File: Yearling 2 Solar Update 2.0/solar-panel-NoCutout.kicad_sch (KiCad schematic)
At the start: 27 parts, among them J1 CON-5040500591, J2 Conn_01x01, J3 Conn_01x01, J4 Conn_01x01, J5 Conn_01x01, U1 APDS-9960, U2 MCP9808_DFN, U3 DRV2605LDGS

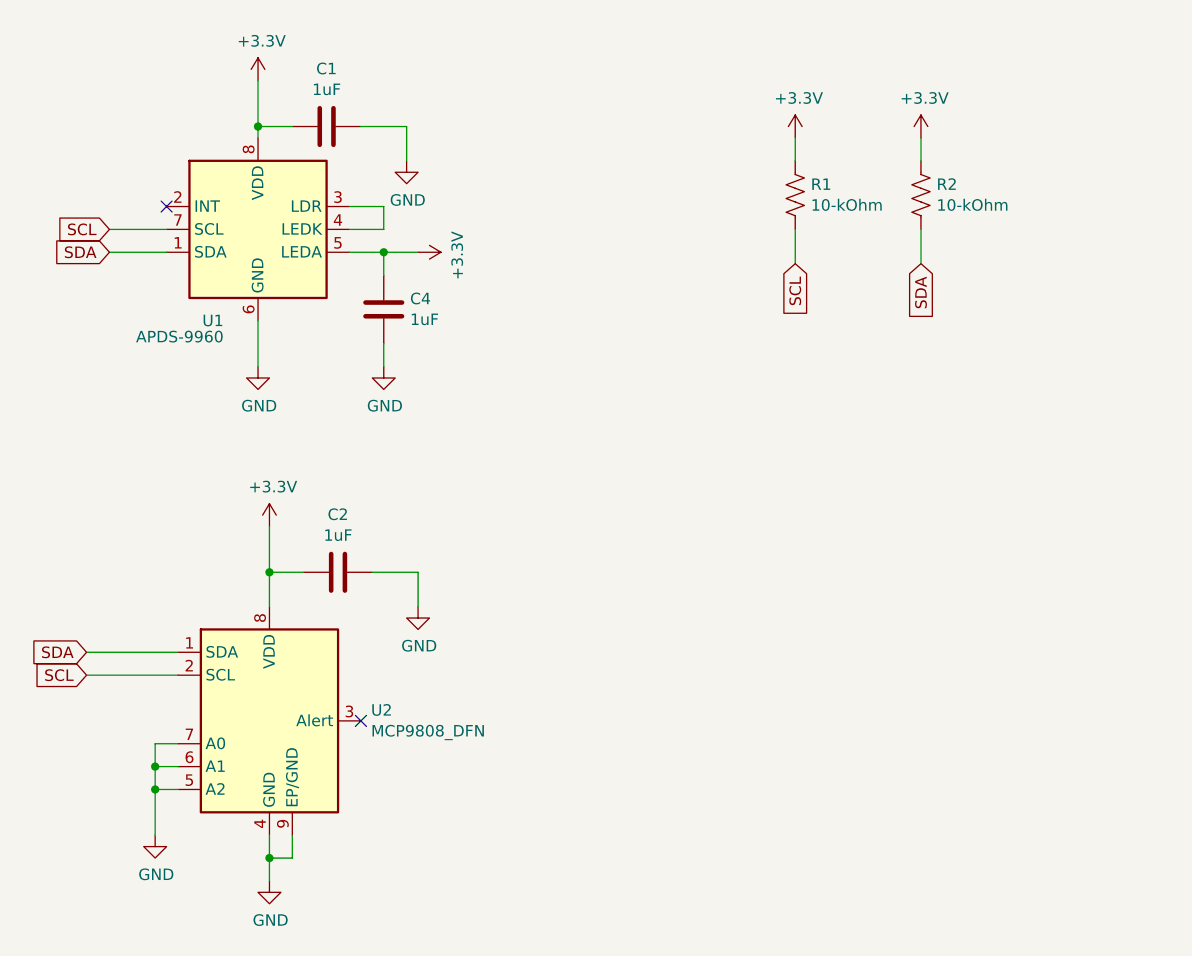
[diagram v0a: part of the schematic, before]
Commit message: Minor Change to light sensor
Replaced APDS part with VLM. Also added LEDS
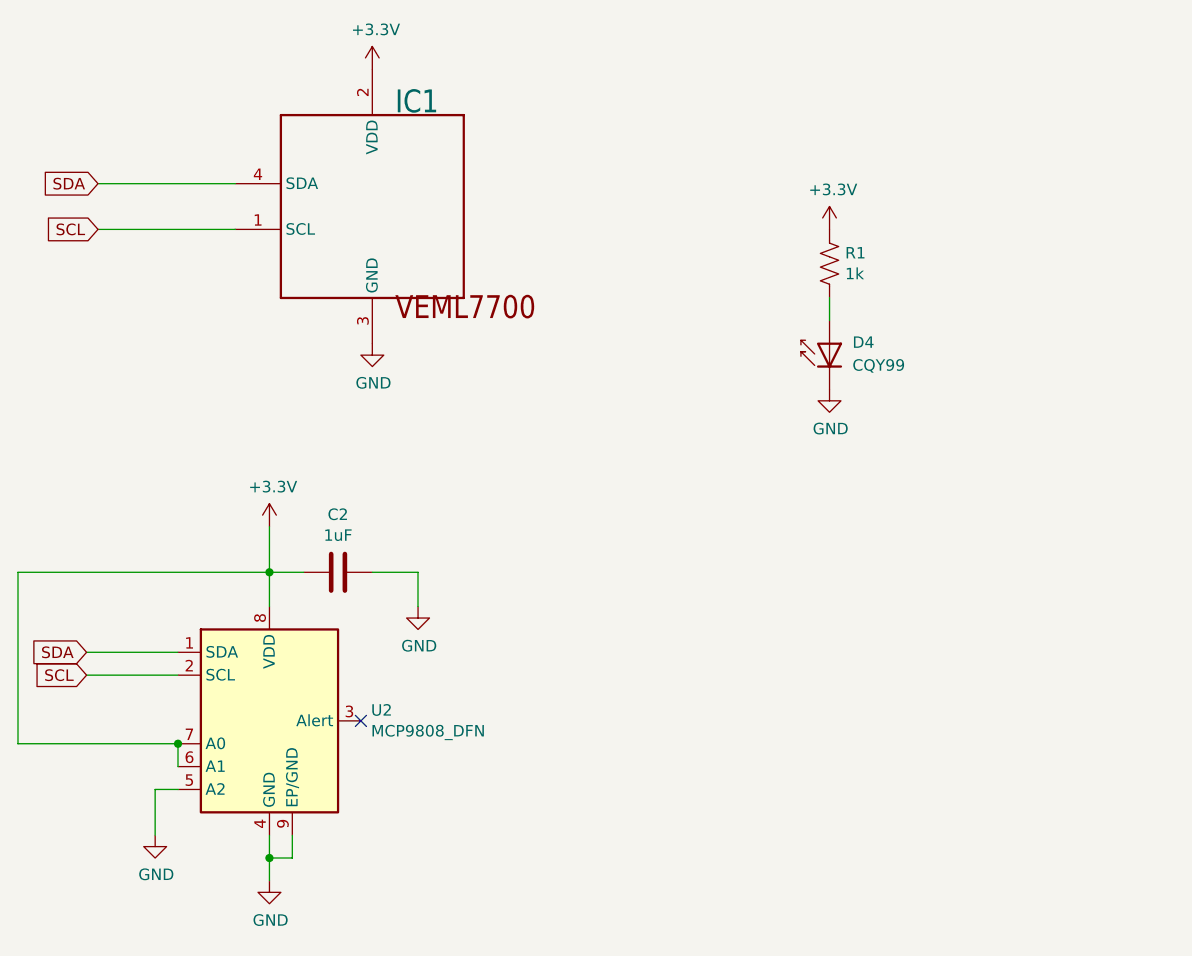
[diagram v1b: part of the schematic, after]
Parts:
- removed C1, C4: 1uF, Capacitor_SMD:C_0805_2012Metric, symbol Device:C
- removed R2: 10-kOhm, Resistor_SMD:R_0603_1608Metric, symbol Device:R_US
- removed U1: APDS-9960, SolarPanelBoards:APDS-9960, symbol XYFaces-rescue:APDS-9960-ExtraComponents
- added D4: CQY99, LED_SMD:LED_0603_1608Metric, symbol LED:CQY99
- added IC1: VEML7700, VEML7700-TT:XDCR_VEML7700-TT, symbol Adafruit VEML7700-eagle-import:VEML7700
- R1: value 10-kOhm -> 1k
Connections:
- net +3V3: now also U2.6 (A1), U2.7 (A0), IC1.2 (VDD)
- net GND: now also D4.1 (K), IC1.3 (GND); no longer U2.6 (A1), U2.7 (A0)
- net SCL: now also IC1.1 (SCL); no longer R1.2
- net SDA: now also IC1.4 (SDA)
- new net: D4.2 (A), R1.2
- no-connect marks 9 -> 8
